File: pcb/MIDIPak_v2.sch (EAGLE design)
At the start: 41 parts, among them IC1 74LS133N, IC3 74LS138N, IC4 68B50, IC5 74LS04N, IC6 74LS161, Q1 4MHz, T1 2N2222/3904, X1 MIDI_IN, X2 MIDI_THRU, X3 MIDI_OUT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

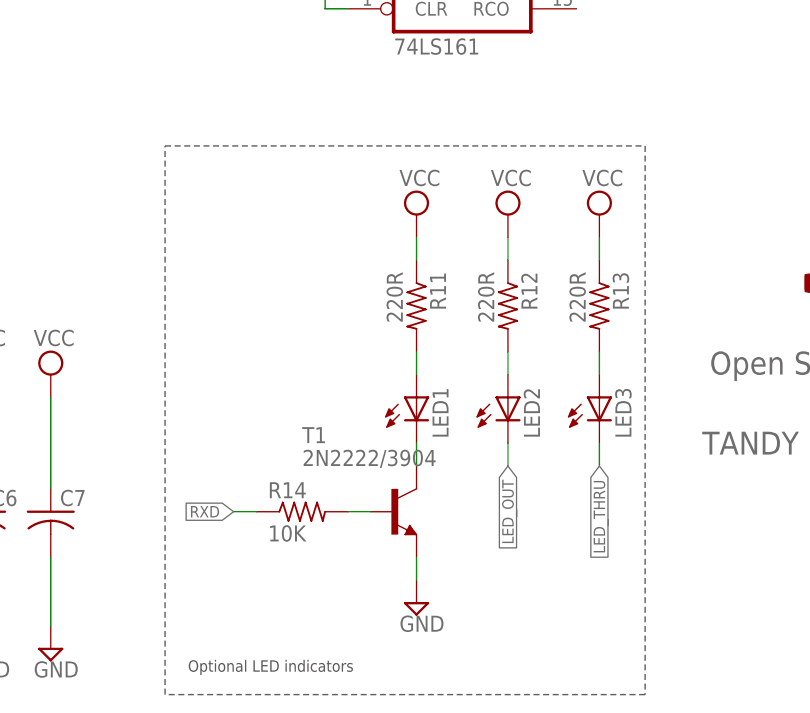
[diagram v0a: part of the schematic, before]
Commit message: Fixed polarity issues with LED signals
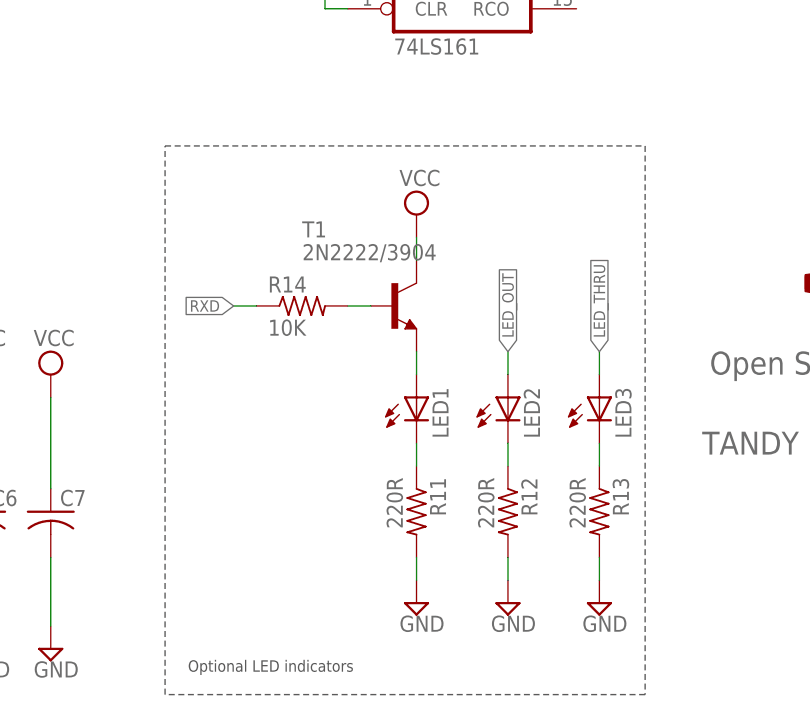
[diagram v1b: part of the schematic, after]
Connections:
- removed net N$25: LED1.A, R11.2
- removed net N$26: LED2.A, R12.2
- removed net N$29: LED3.A, R13.2
- new net N$18: LED2.C, R12.1
- new net N$21: LED1.C, R11.1
- new net N$22: LED3.C, R13.1
- net GND: now also R11.2, R12.2, R13.2; no longer T1.E
- net LED_OUT: now also LED2.A; no longer LED2.C
- net LED_THRU: now also LED3.A; no longer LED3.C
- net N$2: now also LED1.A, T1.E; no longer LED1.C, T1.C
- net VCC: now also T1.C; no longer R11.1, R12.1, R13.1
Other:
- moved on the sheet: R11, R12, R13, R14, T1
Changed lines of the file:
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@@
 <part name="R14" library="resistor" deviceset="R-US_" device="0204/7" value="10K"/>
 <part name="SUPPLY31" library="supply2" deviceset="GND" device=""/>
-<part name="V6" library="supply2" deviceset="VCC" device=""/>
-<part name="V7" library="supply2" deviceset="VCC" device=""/>
-<part name="V8" library="supply2" deviceset="VCC" device=""/>
 <part name="FRAME2" library="frames" deviceset="FRAME_A_L" device=""/>
 <part name="T1" library="transistor" deviceset="2N3904" device="" value="2N2222/3904"/>
@@
 <part name="JP2" library="jumper-jlb" deviceset="JP1Q" device=""/>
 <part name="SUPPLY33" library="supply2" deviceset="GND" device=""/>
+<part name="SUPPLY34" library="supply2" deviceset="GND" device=""/>
+<part name="SUPPLY35" library="supply2" deviceset="GND" device=""/>
+<part name="SUPPLY36" library="supply2" deviceset="VCC" device=""/>
 </parts>
 <sheets>
@@
 <instance part="LED2" gate="G$1" x="154.94" y="35.56"/>
 <instance part="LED3" gate="G$1" x="165.1" y="35.56"/>
-<instance part="R11" gate="G$1" x="144.78" y="45.72" rot="R270"/>
-<instance part="R12" gate="G$1" x="154.94" y="45.72" rot="R270"/>
-<instance part="R13" gate="G$1" x="165.1" y="45.72" rot="R270"/>
-<instance part="R14" gate="G$1" x="132.08" y="22.86"/>
+<instance part="R11" gate="G$1" x="144.78" y="22.86" rot="R270"/>
+<instance part="R12" gate="G$1" x="154.94" y="22.86" rot="R270"/>
+<instance part="R13" gate="G$1" x="165.1" y="22.86" rot="R270"/>
+<instance part="R14" gate="G$1" x="132.08" y="45.72"/>
 <instance part="SUPPLY31" gate="GND" x="144.78" y="12.7"/>
-<instance part="V6" gate="G$1" x="144.78" y="55.88"/>
-<instance part="V7" gate="G$1" x="154.94" y="55.88"/>
-<instance part="V8" gate="G$1" x="165.1" y="55.88"/>
 <instance part="FRAME2" gate="G$1" x="0" y="0"/>
 <instance part="FRAME2" gate="G$2" x="172.72" y="0"/>
-<instance part="T1" gate="G1" x="142.24" y="22.86"/>
+<instance part="T1" gate="G1" x="142.24" y="45.72"/>
 <instance part="JP1" gate="1" x="152.4" y="157.48" rot="MR270"/>
 <instance part="SUPPLY32" gate="GND" x="218.44" y="111.76"/>
 <instance part="JP2" gate="A" x="238.76" y="116.84" rot="R270"/>
 <instance part="SUPPLY33" gate="GND" x="248.92" y="111.76"/>
+<instance part="SUPPLY34" gate="GND" x="165.1" y="12.7"/>
+<instance part="SUPPLY35" gate="GND" x="154.94" y="12.7"/>
+<instance part="SUPPLY36" gate="G$1" x="144.78" y="55.88"/>
 </instances>
 <busses>
@@
 </segment>
 <segment>
-<pinref part="SUPPLY31" gate="GND" pin="GND"/>
-<wire x1="144.78" y1="17.78" x2="144.78" y2="15.24" width="0.1524" layer="91"/>
-<pinref part="T1" gate="G1" pin="E"/>
-</segment>
-<segment>
 <pinref part="SUPPLY33" gate="GND" pin="GND"/>
 <wire x1="248.92" y1="114.3" x2="248.92" y2="116.84" width="0.1524" layer="91"/>
 <pinref part="JP2" gate="A" pin="2"/>
 <wire x1="248.92" y1="116.84" x2="246.38" y2="116.84" width="0.1524" layer="91"/>
+</segment>
+<segment>
+<pinref part="R13" gate="G$1" pin="2"/>
+<pinref part="SUPPLY34" gate="GND" pin="GND"/>
+<wire x1="165.1" y1="17.78" x2="165.1" y2="15.24" width="0.1524" layer="91"/>
+</segment>
+<segment>
+<pinref part="R12" gate="G$1" pin="2"/>
+<pinref part="SUPPLY35" gate="GND" pin="GND"/>
+<wire x1="154.94" y1="17.78" x2="154.94" y2="15.24" width="0.1524" layer="91"/>
+</segment>
+<segment>
+<pinref part="R11" gate="G$1" pin="2"/>
+<pinref part="SUPPLY31" gate="GND" pin="GND"/>
+<wire x1="144.78" y1="17.78" x2="144.78" y2="15.24" width="0.1524" layer="91"/>
 </segment>
 </net>
@@
 </segment>
 <segment>
-<pinref part="R12" gate="G$1" pin="1"/>
-<wire x1="154.94" y1="50.8" x2="154.94" y2="53.34" width="0.1524" layer="91"/>
-<pinref part="V7" gate="G$1" pin="VCC"/>
-</segment>
-<segment>
-<pinref part="R13" gate="G$1" pin="1"/>
-<wire x1="165.1" y1="50.8" x2="165.1" y2="53.34" width="0.1524" layer="91"/>
-<pinref part="V8" gate="G$1" pin="VCC"/>
-</segment>
-<segment>
-<pinref part="V6" gate="G$1" pin="VCC"/>
-<pinref part="R11" gate="G$1" pin="1"/>
+<pinref part="SUPPLY36" gate="G$1" pin="VCC"/>
+<pinref part="T1" gate="G1" pin="C"/>
 <wire x1="144.78" y1="53.34" x2="144.78" y2="50.8" width="0.1524" layer="91"/>
 </segment>
@@
 <segment>
 <pinref part="R14" gate="G$1" pin="1"/>
-<wire x1="127" y1="22.86" x2="124.46" y2="22.86" width="0.1524" layer="91"/>
-<label x="124.46" y="22.86" size="1.27" layer="95" ratio="10" rot="R180" xref="yes"/>
+<wire x1="127" y1="45.72" x2="124.46" y2="45.72" width="0.1524" layer="91"/>
+<label x="124.46" y="45.72" size="1.27" layer="95" ratio="10" rot="R180" xref="yes"/>
 </segment>
 </net>
@@
 <segment>
 <pinref part="R14" gate="G$1" pin="2"/>
-<wire x1="137.16" y1="22.86" x2="139.7" y2="22.86" width="0.1524" layer="91"/>
+<wire x1="137.16" y1="45.72" x2="139.7" y2="45.72" width="0.1524" layer="91"/>
 <pinref part="T1" gate="G1" pin="B"/>
 </segment>
 </net>
-<net name="N$25" class="0">
-<segment>
-<pinref part="R11" gate="G$1" pin="2"/>
-<pinref part="LED1" gate="G$1" pin="A"/>
-<wire x1="144.78" y1="40.64" x2="144.78" y2="38.1" width="0.1524" layer="91"/>
-</segment>
-</net>
-<net name="N$26" class="0">
-<segment>
-<pinref part="R12" gate="G$1" pin="2"/>
+<net name="LED_OUT" class="0">
+<segment>
+<label x="154.94" y="40.64" size="1.27" layer="95" ratio="10" rot="R90" xref="yes"/>
 <pinref part="LED2" gate="G$1" pin="A"/>
 <wire x1="154.94" y1="40.64" x2="154.94" y2="38.1" width="0.1524" layer="91"/>
-</segment>
-</net>
-<net name="N$29" class="0">
-<segment>
-<pinref part="R13" gate="G$1" pin="2"/>
-<pinref part="LED3" gate="G$1" pin="A"/>
-<wire x1="165.1" y1="40.64" x2="165.1" y2="38.1" width="0.1524" layer="91"/>
-</segment>
-</net>
-<net name="LED_OUT" class="0">
-<segment>
-<pinref part="LED2" gate="G$1" pin="C"/>
-<wire x1="154.94" y1="30.48" x2="154.94" y2="27.94" width="0.1524" layer="91"/>
-<label x="154.94" y="27.94" size="1.27" layer="95" ratio="10" rot="R270" xref="yes"/>
 </segment>
 <segment>
@@
 <net name="LED_THRU" class="0">
 <segment>
-<pinref part="LED3" gate="G$1" pin="C"/>
-<wire x1="165.1" y1="30.48" x2="165.1" y2="27.94" width="0.1524" layer="91"/>
-<label x="165.1" y="27.94" size="1.27" layer="95" ratio="10" rot="R270" xref="yes"/>
+<label x="165.1" y="40.64" size="1.27" layer="95" ratio="10" rot="R90" xref="yes"/>
+<pinref part="LED3" gate="G$1" pin="A"/>
+<wire x1="165.1" y1="40.64" x2="165.1" y2="38.1" width="0.1524" layer="91"/>
 </segment>
 <segment>
@@
 <junction x="180.34" y="157.48"/>
 <label x="180.34" y="160.02" size="1.27" layer="95" ratio="10" rot="R90" xref="yes"/>
-</segment>
-</net>
-<net name="N$2" class="0">
-<segment>
-<pinref part="LED1" gate="G$1" pin="C"/>
-<wire x1="144.78" y1="30.48" x2="144.78" y2="27.94" width="0.1524" layer="91"/>
-<pinref part="T1" gate="G1" pin="C"/>
 </segment>
 </net>
@@
 </segment>
 </net>
+<net name="N$22" class="0">
+<segment>
+<pinref part="R13" gate="G$1" pin="1"/>
+<wire x1="165.1" y1="27.94" x2="165.1" y2="30.48" width="0.1524" layer="91"/>
+<pinref part="LED3" gate="G$1" pin="C"/>
+</segment>
+</net>
+<net name="N$18" class="0">
+<segment>
+<pinref part="R12" gate="G$1" pin="1"/>
+<pinref part="LED2" gate="G$1" pin="C"/>
+<wire x1="154.94" y1="30.48" x2="154.94" y2="27.94" width="0.1524" layer="91"/>
+</segment>
+</net>
+<net name="N$2" class="0">
+<segment>
+<pinref part="T1" gate="G1" pin="E"/>
+<pinref part="LED1" gate="G$1" pin="A"/>
+<wire x1="144.78" y1="40.64" x2="144.78" y2="38.1" width="0.1524" layer="91"/>
+</segment>
+</net>
+<net name="N$21" class="0">
+<segment>
+<pinref part="LED1" gate="G$1" pin="C"/>
+<pinref part="R11" gate="G$1" pin="1"/>
+<wire x1="144.78" y1="30.48" x2="144.78" y2="27.94" width="0.1524" layer="91"/>
+</segment>
+</net>
